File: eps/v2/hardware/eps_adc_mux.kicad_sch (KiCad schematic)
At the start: 11 parts, among them U1 ADS124S08IPBSR

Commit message: rebase ADC Mux
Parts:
- renumbered C1 to C10, C3 to C11, C2 to C12, R6 to R40, R5 to R41, R4 to R42, R9 to R43, R10 to R44, R8 to R45, R7 to R46, U1 to U4
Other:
- removed sheet Inter-Board-Connector
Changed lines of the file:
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@@
 		(in_pos_files yes)
 		(dnp no)
-		(property "Reference" "C3"
+		(property "Reference" "C11"
 			(at 105.918 138.684 0)
 			(show_name no)
@@
 		)
 		(instances
-			(project "eps_adc_mux"
+			(project "eps"
 				(path "/b20f5a9e-495e-48d8-8648-bd5c7d9b4620"
 					(reference "C3")
+					(unit 1)
+				)
+				(path "/b20f5a9e-495e-48d8-8648-bd5c7d9b4620/1db763c0-7203-4e82-a960-796c90813502"
+					(reference "C11")
 					(unit 1)
 				)
@@
 		(in_pos_files yes)
 		(dnp no)
-		(property "Reference" "R9"
+		(property "Reference" "R43"
 			(at 176.53 91.44 90)
 			(show_name no)
@@
 		)
 		(instances
-			(project "eps_adc_mux"
+			(project "eps"
 				(path "/b20f5a9e-495e-48d8-8648-bd5c7d9b4620"
 					(reference "R9")
+					(unit 1)
+				)
+				(path "/b20f5a9e-495e-48d8-8648-bd5c7d9b4620/1db763c0-7203-4e82-a960-796c90813502"
+					(reference "R43")
 					(unit 1)
 				)
@@
 		(dnp no)
 		(fields_autoplaced yes)
-		(property "Reference" "U1"
+		(property "Reference" "U4"
 			(at 143.51 60.96 0)
 			(show_name no)
@@
 		)
 		(instances
-			(project "eps_adc_mux"
+			(project "eps"
 				(path "/b20f5a9e-495e-48d8-8648-bd5c7d9b4620"
 					(reference "U1")
+					(unit 1)
+				)
+				(path "/b20f5a9e-495e-48d8-8648-bd5c7d9b4620/1db763c0-7203-4e82-a960-796c90813502"
+					(reference "U4")
 					(unit 1)
 				)
@@
 		(in_pos_files yes)
 		(dnp no)
-		(property "Reference" "R6"
+		(property "Reference" "R40"
 			(at 176.53 73.66 90)
 			(show_name no)
@@
 		)
 		(instances
-			(project "eps_adc_mux"
+			(project "eps"
 				(path "/b20f5a9e-495e-48d8-8648-bd5c7d9b4620"
 					(reference "R6")
+					(unit 1)
+				)
+				(path "/b20f5a9e-495e-48d8-8648-bd5c7d9b4620/1db763c0-7203-4e82-a960-796c90813502"
+					(reference "R40")
 					(unit 1)
 				)
@@
 		(in_pos_files yes)
 		(dnp no)
-		(property "Reference" "R7"
+		(property "Reference" "R46"
 			(at 184.15 77.47 90)
 			(show_name no)
@@
 		)
 		(instances
-			(project "eps_adc_mux"
+			(project "eps"
 				(path "/b20f5a9e-495e-48d8-8648-bd5c7d9b4620"
 					(reference "R7")
+					(unit 1)
+				)
+				(path "/b20f5a9e-495e-48d8-8648-bd5c7d9b4620/1db763c0-7203-4e82-a960-796c90813502"
+					(reference "R46")
 					(unit 1)
 				)
@@
 		)
 		(instances
-			(project "eps_adc_mux"
-				(path "/b20f5a9e-495e-48d8-8648-bd5c7d9b4620"
+			(project "eps"
+				(path "/b20f5a9e-495e-48d8-8648-bd5c7d9b4620"
+					(reference "#PWR09")
+					(unit 1)
+				)
+				(path "/b20f5a9e-495e-48d8-8648-bd5c7d9b4620/1db763c0-7203-4e82-a960-796c90813502"
 					(reference "#PWR09")
 					(unit 1)
@@
 		)
 		(instances
-			(project "eps_adc_mux"
-				(path "/b20f5a9e-495e-48d8-8648-bd5c7d9b4620"
+			(project "eps"
+				(path "/b20f5a9e-495e-48d8-8648-bd5c7d9b4620"
+					(reference "#PWR010")
+					(unit 1)
+				)
+				(path "/b20f5a9e-495e-48d8-8648-bd5c7d9b4620/1db763c0-7203-4e82-a960-796c90813502"
 					(reference "#PWR010")
 					(unit 1)
@@
 		(in_pos_files yes)
 		(dnp no)
-		(property "Reference" "R8"
+		(property "Reference" "R45"
 			(at 184.15 69.85 90)
 			(show_name no)
@@
 		)
 		(instances
-			(project "eps_adc_mux"
+			(project "eps"
 				(path "/b20f5a9e-495e-48d8-8648-bd5c7d9b4620"
 					(reference "R8")
+					(unit 1)
+				)
+				(path "/b20f5a9e-495e-48d8-8648-bd5c7d9b4620/1db763c0-7203-4e82-a960-796c90813502"
+					(reference "R45")
 					(unit 1)
 				)
@@
 		(in_pos_files yes)
 		(dnp no)
-		(property "Reference" "C1"
+		(property "Reference" "C10"
 			(at 100.838 84.582 90)
 			(show_name no)
@@
 		)
 		(instances
-			(project "eps_adc_mux"
+			(project "eps"
 				(path "/b20f5a9e-495e-48d8-8648-bd5c7d9b4620"
 					(reference "C1")
+					(unit 1)
+				)
+				(path "/b20f5a9e-495e-48d8-8648-bd5c7d9b4620/1db763c0-7203-4e82-a960-796c90813502"
+					(reference "C10")
 					(unit 1)
 				)
@@
 		)
 		(instances
-			(project "eps_adc_mux"
-				(path "/b20f5a9e-495e-48d8-8648-bd5c7d9b4620"
+			(project "eps"
+				(path "/b20f5a9e-495e-48d8-8648-bd5c7d9b4620"
+					(reference "#PWR08")
+					(unit 1)
+				)
+				(path "/b20f5a9e-495e-48d8-8648-bd5c7d9b4620/1db763c0-7203-4e82-a960-796c90813502"
 					(reference "#PWR08")
 					(unit 1)
@@
 		(in_pos_files yes)
 		(dnp no)
-		(property "Reference" "R10"
+		(property "Reference" "R44"
 			(at 176.53 96.52 90)
 			(show_name no)
@@
 		)
 		(instances
-			(project "eps_adc_mux"
+			(project "eps"
 				(path "/b20f5a9e-495e-48d8-8648-bd5c7d9b4620"
 					(reference "R10")
+					(unit 1)
+				)
+				(path "/b20f5a9e-495e-48d8-8648-bd5c7d9b4620/1db763c0-7203-4e82-a960-796c90813502"
+					(reference "R44")
 					(unit 1)
 				)
@@
 		(in_pos_files yes)
 		(dnp no)
-		(property "Reference" "R5"
+		(property "Reference" "R41"
 			(at 176.53 81.28 90)
 			(show_name no)
@@
 		)
 		(instances
-			(project "eps_adc_mux"
+			(project "eps"
 				(path "/b20f5a9e-495e-48d8-8648-bd5c7d9b4620"
 					(reference "R5")
+					(unit 1)
+				)
+				(path "/b20f5a9e-495e-48d8-8648-bd5c7d9b4620/1db763c0-7203-4e82-a960-796c90813502"
+					(reference "R41")
 					(unit 1)
 				)
@@
 		)
 		(instances
-			(project "eps_adc_mux"
-				(path "/b20f5a9e-495e-48d8-8648-bd5c7d9b4620"
+			(project "eps"
+				(path "/b20f5a9e-495e-48d8-8648-bd5c7d9b4620"
+					(reference "#PWR011")
+					(unit 1)
+				)
+				(path "/b20f5a9e-495e-48d8-8648-bd5c7d9b4620/1db763c0-7203-4e82-a960-796c90813502"
 					(reference "#PWR011")
 					(unit 1)
@@
 		(in_pos_files yes)
 		(dnp no)
-		(property "Reference" "R4"
+		(property "Reference" "R42"
 			(at 176.53 86.36 90)
 			(show_name no)
@@
 		)
 		(instances
-			(project "eps_adc_mux"
+			(project "eps"
 				(path "/b20f5a9e-495e-48d8-8648-bd5c7d9b4620"
 					(reference "R4")
+					(unit 1)
+				)
+				(path "/b20f5a9e-495e-48d8-8648-bd5c7d9b4620/1db763c0-7203-4e82-a960-796c90813502"
+					(reference "R42")
 					(unit 1)
 				)
@@
 		(dnp no)
 		(fields_autoplaced yes)
-		(property "Reference" "C2"
+		(property "Reference" "C12"
 			(at 179.07 123.0629 0)
 			(show_name no)
@@
 		)
 		(instances
-			(project "eps_adc_mux"
+			(project "eps"
 				(path "/b20f5a9e-495e-48d8-8648-bd5c7d9b4620"
 					(reference "C2")
 					(unit 1)
 				)
-			)
-		)
-	)
-	(sheet
-		(at 15.24 149.86)
-		(size 45.085 44.45)
-		(exclude_from_sim no)
-		(in_bom yes)
-		(on_board yes)
-		(dnp no)
-		(fields_autoplaced yes)
-		(stroke
-			(width 0.1524)
-			(type solid)
-		)
-		(fill
-			(color 0 0 0 0)
-		)
-		(property "Sheetname" "Inter-Board-Connector"
-			(at 15.24 149.1484 0)
-			(show_name no)
-			(do_not_autoplace no)
-			(effects
-				(font
-					(size 1.27 1.27)
-				)
-				(justify left bottom)
-			)
-		)
-		(property "Sheetfile" "inter_board_connector.kicad_sch"
-			(at 15.24 194.8946 0)
-			(show_name no)
-			(do_not_autoplace no)
-			(effects
-				(font
-					(size 1.27 1.27)
-				)
-				(justify left top)
-			)
-		)
-		(instances
-			(project "eps_adc_mux"
-				(path "/b20f5a9e-495e-48d8-8648-bd5c7d9b4620"
-					(page "2")
-				)
-			)
-		)
-	)
-	(sheet_instances
-		(path "/"
-			(page "1")
-		)
-	)
-	(embedded_fonts no)
+				(path "/b20f5a9e-495e-48d8-8648-bd5c7d9b4620/1db763c0-7203-4e82-a960-796c90813502"
+					(reference "C12")
+					(unit 1)
+				)
+			)
+		)
+	)
 )

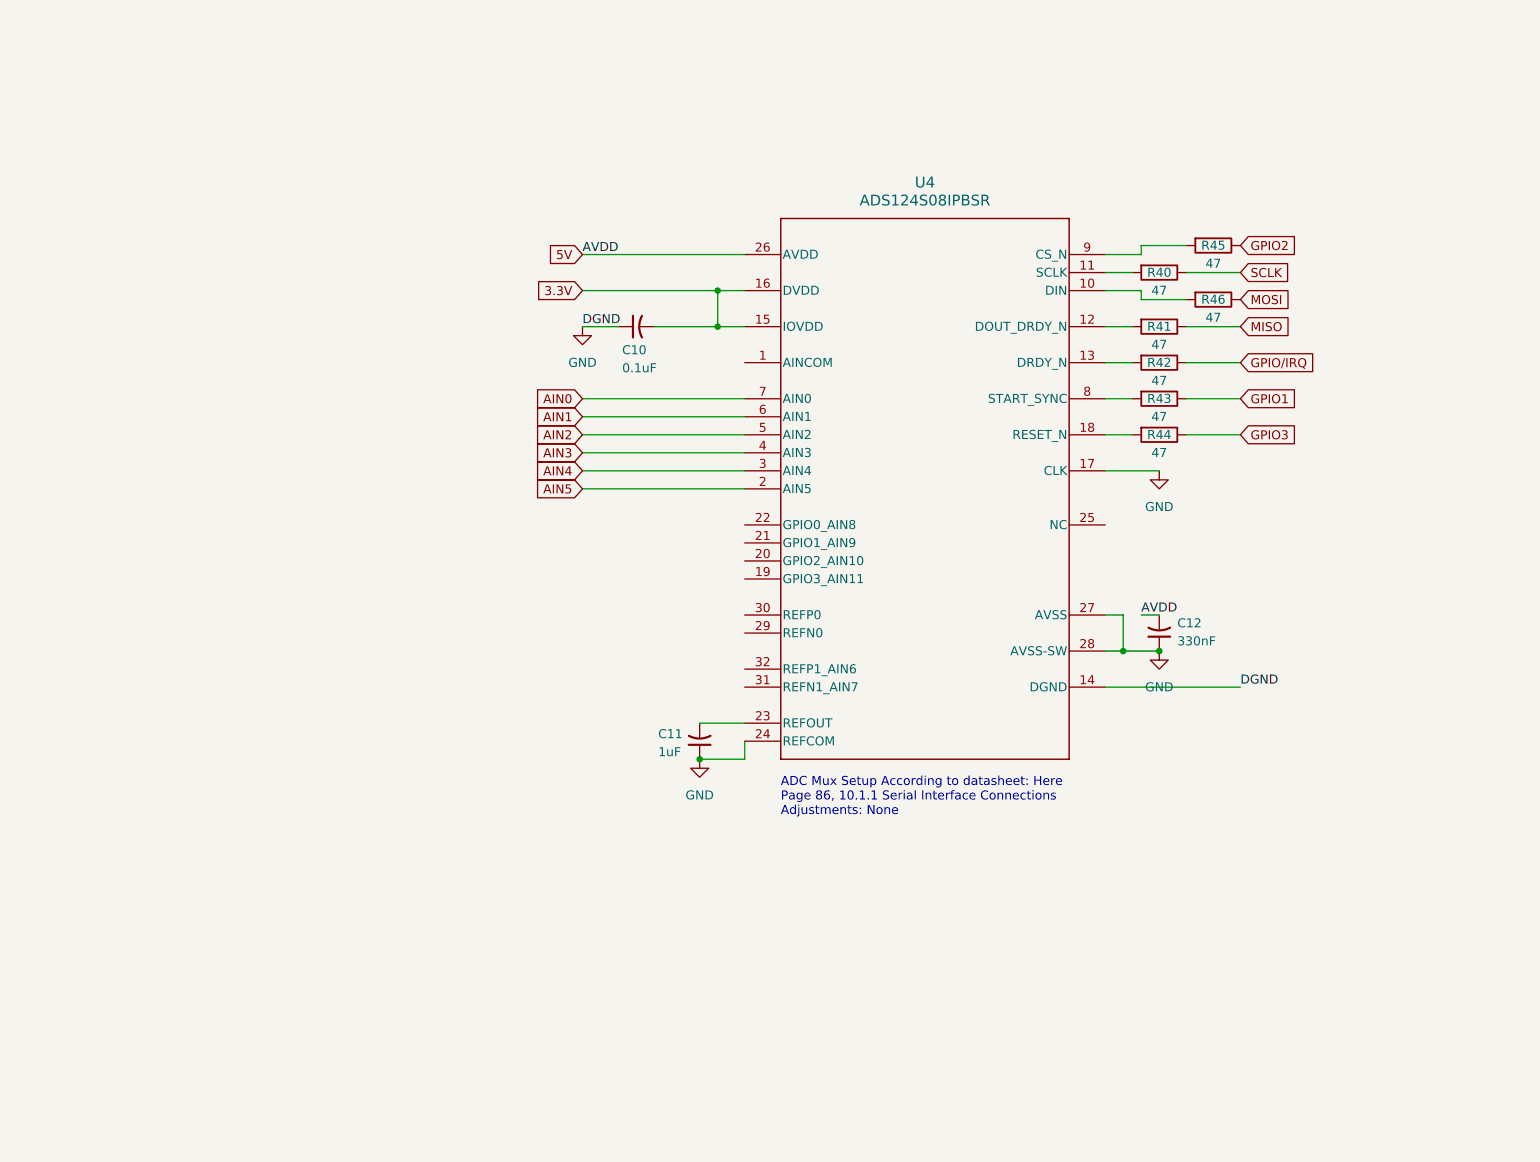
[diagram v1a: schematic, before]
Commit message: ADS124S08: Sym, Fp, Sch
-Redid the symbol
-Linked previous footprint (steven)
-Implemented sub sheet
-Fixed incorrect file hierarchy
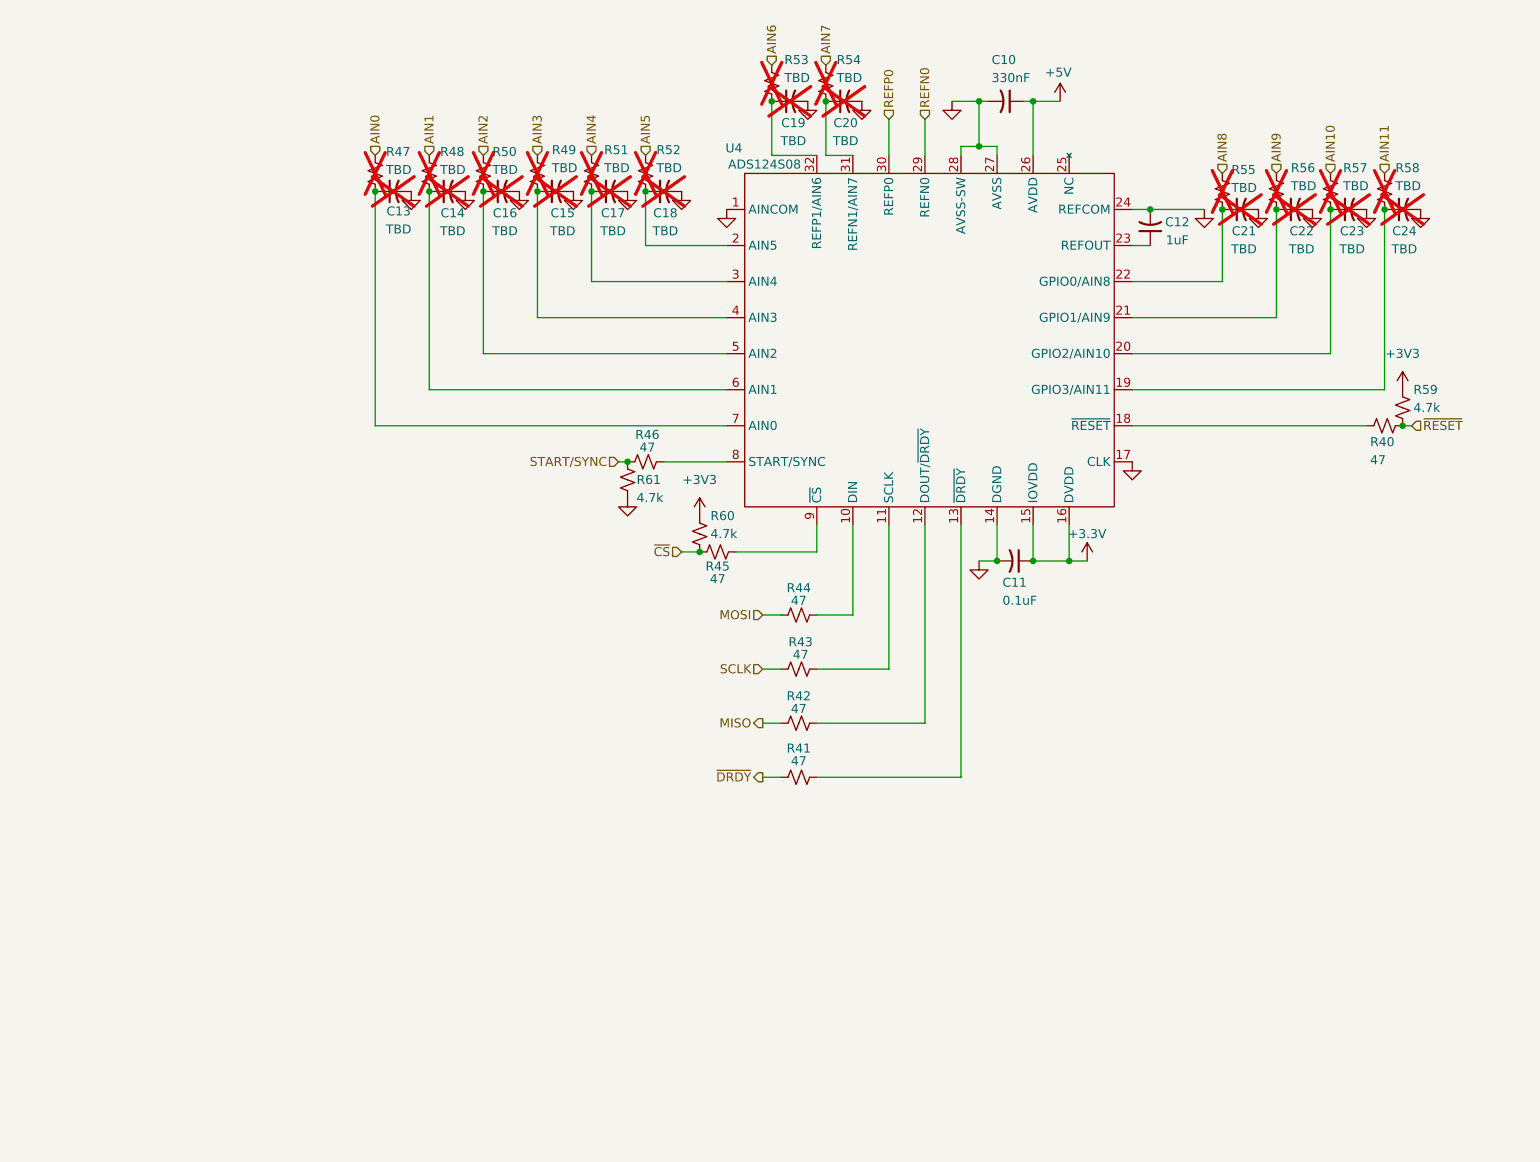
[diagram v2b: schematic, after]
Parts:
- removed R40, R41, R42, R43, R44, R45, R46: 47, PBS0032A_N, symbol Device:R
- removed U4: ADS124S08IPBSR, PBS0032A_N, symbol OSUSAT:ADS124S08IPBSR
- added C13, C14, C15, C16, C17, C18, C19, C20, C21, C22, C23, C24: TBD, symbol Device:C_Small_US
- added R40, R41, R42, R43, R44, R45, R46: 47, symbol Device:R_Small_US
- added R47, R48, R49, R50, R51, R52, R53, R54, R55, R56, R57, R58: TBD, symbol Device:R_Small_US
- added R59, R60, R61: 4.7k, symbol Device:R_Small_US
- added U4: ADS124S08, OSUSAT_ICs:PBS0032A_N, symbol OSUSAT_EPS:ADS124S08
- C10: value 0.1uF -> 330nF; footprint Package_SO:SOIC-8_3.9x4.9mm_P1.27mm -> (none)
- C11: value 1uF -> 0.1uF
- C12: value 330nF -> 1uF
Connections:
- net 3.3V is gone; now on net GND: C10.2
- net 5V is gone; now on net GND: C12.2
- net AIN0: now also R47.1
- net AIN1: now also R48.1
- net AIN2: now also R50.1
- net AIN3: now also R49.1
- net AIN4: now also R51.1
- net AIN5: now also R52.1
- net GND: now also C11.2, C13.2, C14.2, C15.2, C16.2, C17.2, C18.2, C19.2, C20.2, C21.2, C22.2, C23.2, C24.2, R61.2, U4.1 (AINCOM), U4.14 (DGND), U4.17 (CLK), U4.24 (REFCOM), U4.27 (AVSS), U4.28 (AVSS-SW); no longer C10.1, C11.1, C12.1
- net MISO: now also R42.2
- net MOSI: now also R44.2
- net SCLK: now also R43.2
- new net: C21.1, R55.2, U4.22 (GPIO0/AIN8)
- new net: C19.1, R53.2, U4.32 (REFP1/AIN6)
- new net: C22.1, R56.2, U4.21 (GPIO1/AIN9)
- new net: R41.1, U4.13 (~{DRDY})
- new net: C24.1, R58.2, U4.19 (GPIO3/AIN11)
- new net: C16.1, R50.2, U4.5 (AIN2)
- new net: C18.1, R52.2, U4.2 (AIN5)
- new net: C17.1, R51.2, U4.3 (AIN4)
- new net: C23.1, R57.2, U4.20 (GPIO2/AIN10)
- new net: C14.1, R48.2, U4.6 (AIN1)
- new net: C12.1, U4.23 (REFOUT)
- new net: C15.1, R49.2, U4.4 (AIN3)
- new net: C13.1, R47.2, U4.7 (AIN0)
- new net: R43.1, U4.11 (SCLK)
- new net: C20.1, R54.2, U4.31 (REFN1/AIN7)
- new net: R45.2, U4.9 (~{CS})
- new net: R40.2, U4.18 (~{RESET})
- new net: R44.1, U4.10 (DIN)
- new net: R42.1, U4.12 (DOUT/~{DRDY})
- new net: R46.1, U4.8 (START/SYNC)
- new net +3.3V: C11.1, U4.15 (IOVDD), U4.16 (DVDD)
- new net +3V3: R59.1, R60.1
- new net +5V: C10.1, U4.26 (AVDD)
- new net AIN10: R57.1
- new net AIN11: R58.1
- new net AIN6: R53.1
- new net AIN7: R54.1
- new net AIN8: R55.1
- new net AIN9: R56.1
- new net REFN0: U4.29 (REFN0)
- new net REFP0: U4.30 (REFP0)
- new net START/SYNC: R46.2, R61.1
- new net ~{CS}: R45.1, R60.2
- new net ~{DRDY}: R41.2
- new net ~{RESET}: R40.1, R59.2
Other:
- note removed: "ADC Mux Setup According to datasheet: Here Page 86, 10.1.1 Serial Interface Connections Adjustments: None"
